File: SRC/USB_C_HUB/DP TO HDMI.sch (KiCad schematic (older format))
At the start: 3 parts

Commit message: ALL DONE BUT THE HDMI SECTION. NEED FOOTPRINT ASSIGNMENT
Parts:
- D11: renamed from D?; footprint DMX0003A -> SamacSys_Parts_2:DMX0003A
- IC2: renamed from IC?; footprint QFN50P700X700X80-49N -> SamacSys_Parts_2:QFN50P700X700X80-49N
- gave numbers to parts that had none: 1
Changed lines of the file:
@@
 $Descr A4 11693 8268
 encoding utf-8
-Sheet 8 11
+Sheet 4 15
 Title ""
 Date ""
@@
 AR Path="/619540C6/64E7C5EF" Ref="#PWR?"  Part="1"
 AR Path="/64E7C5EF" Ref="#PWR?"  Part="1"
-AR Path="/64E160D5/64E7C5EF" Ref="#PWR?"  Part="1"
-F 0 "#PWR?" H 6150 2900 50  0001 C CNN
+AR Path="/64E160D5/64E7C5EF" Ref="#PWR0149"  Part="1"
+F 0 "#PWR0149" H 6150 2900 50  0001 C CNN
 F 1 "GND" H 6155 2977 50  0000 C CNN
 F 2 "" H 6150 3150 60  0000 C CNN
@@
 P 6225 3150
 AR Path="/64E7C5FE" Ref="D?"  Part="1"
-AR Path="/64E160D5/64E7C5FE" Ref="D?"  Part="1"
-F 0 "D?" H 6125 3075 50  0000 C CNN
+AR Path="/64E160D5/64E7C5FE" Ref="D11"  Part="1"
+F 0 "D11" H 6125 3075 50  0000 C CNN
 F 1 "ESD122DMXR" H 6125 3000 50  0000 C CNN
-F 2 "DMX0003A" H 7075 3250 50  0001 L CNN
+F 2 "SamacSys_Parts_2:DMX0003A" H 7075 3250 50  0001 L CNN
 F 3 "http://www.ti.com/lit/gpn/esd122" H 7075 3150 50  0001 L CNN
 F 4 "2-Channel ESD Protection Diode for USB Type-C and HDMI 2.0" H 7075 3050 50  0001 L CNN "Description"
@@
 P 8175 3625
 AR Path="/64E7C620" Ref="#PWR?"  Part="1"
-AR Path="/64E160D5/64E7C620" Ref="#PWR?"  Part="1"
-F 0 "#PWR?" H 8175 3475 50  0001 C CNN
+AR Path="/64E160D5/64E7C620" Ref="#PWR0150"  Part="1"
+F 0 "#PWR0150" H 8175 3475 50  0001 C CNN
 F 1 "+5V" V 8190 3753 50  0000 L CNN
 F 2 "" H 8175 3625 60  0000 C CNN
@@
 P 8575 2850
 AR Path="/64E7C627" Ref="HDMI?"  Part="1"
-AR Path="/64E160D5/64E7C627" Ref="HDMI?"  Part="1"
-F 0 "HDMI?" H 8431 2804 50  0000 R CNN
+AR Path="/64E160D5/64E7C627" Ref="HDMI1"  Part="1"
+F 0 "HDMI1" H 8431 2804 50  0000 R CNN
 F 1 "HDMI-SWM-19" H 8431 2895 50  0000 R CNN
 F 2 "" H 8605 3000 20  0001 C CNN
@@
 P 8900 1775
 AR Path="/64E7C634" Ref="#PWR?"  Part="1"
-AR Path="/64E160D5/64E7C634" Ref="#PWR?"  Part="1"
-F 0 "#PWR?" H 8900 1525 50  0001 C CNN
+AR Path="/64E160D5/64E7C634" Ref="#PWR0151"  Part="1"
+F 0 "#PWR0151" H 8900 1525 50  0001 C CNN
 F 1 "GND" H 8905 1602 50  0000 C CNN
 F 2 "" H 8900 1775 60  0000 C CNN
@@
 P 8625 4025
 AR Path="/64E7C63A" Ref="#PWR?"  Part="1"
-AR Path="/64E160D5/64E7C63A" Ref="#PWR?"  Part="1"
-F 0 "#PWR?" H 8625 3775 50  0001 C CNN
+AR Path="/64E160D5/64E7C63A" Ref="#PWR0152"  Part="1"
+F 0 "#PWR0152" H 8625 3775 50  0001 C CNN
 F 1 "GND" H 8725 3900 50  0000 C CNN
 F 2 "" H 8625 4025 60  0000 C CNN
@@
 P 3200 4075
 AR Path="/64E7C666" Ref="IC?"  Part="1"
-AR Path="/64E160D5/64E7C666" Ref="IC?"  Part="1"
-F 0 "IC?" V 4150 3550 50  0000 C CNN
+AR Path="/64E160D5/64E7C666" Ref="IC2"  Part="1"
+F 0 "IC2" V 4150 3550 50  0000 C CNN
 F 1 "MAX9406ETM+T" V 4025 3500 50  0000 C CNN
-F 2 "QFN50P700X700X80-49N" H 4850 4575 50  0001 L CNN
+F 2 "SamacSys_Parts_2:QFN50P700X700X80-49N" H 4850 4575 50  0001 L CNN
 F 3 "https://pdfserv.maximintegrated.com/en/ds/MAX9406.pdf" H 4850 4475 50  0001 L CNN
 F 4 "MAX9406ETM+T" H 4850 4375 50  0001 L CNN "Description"

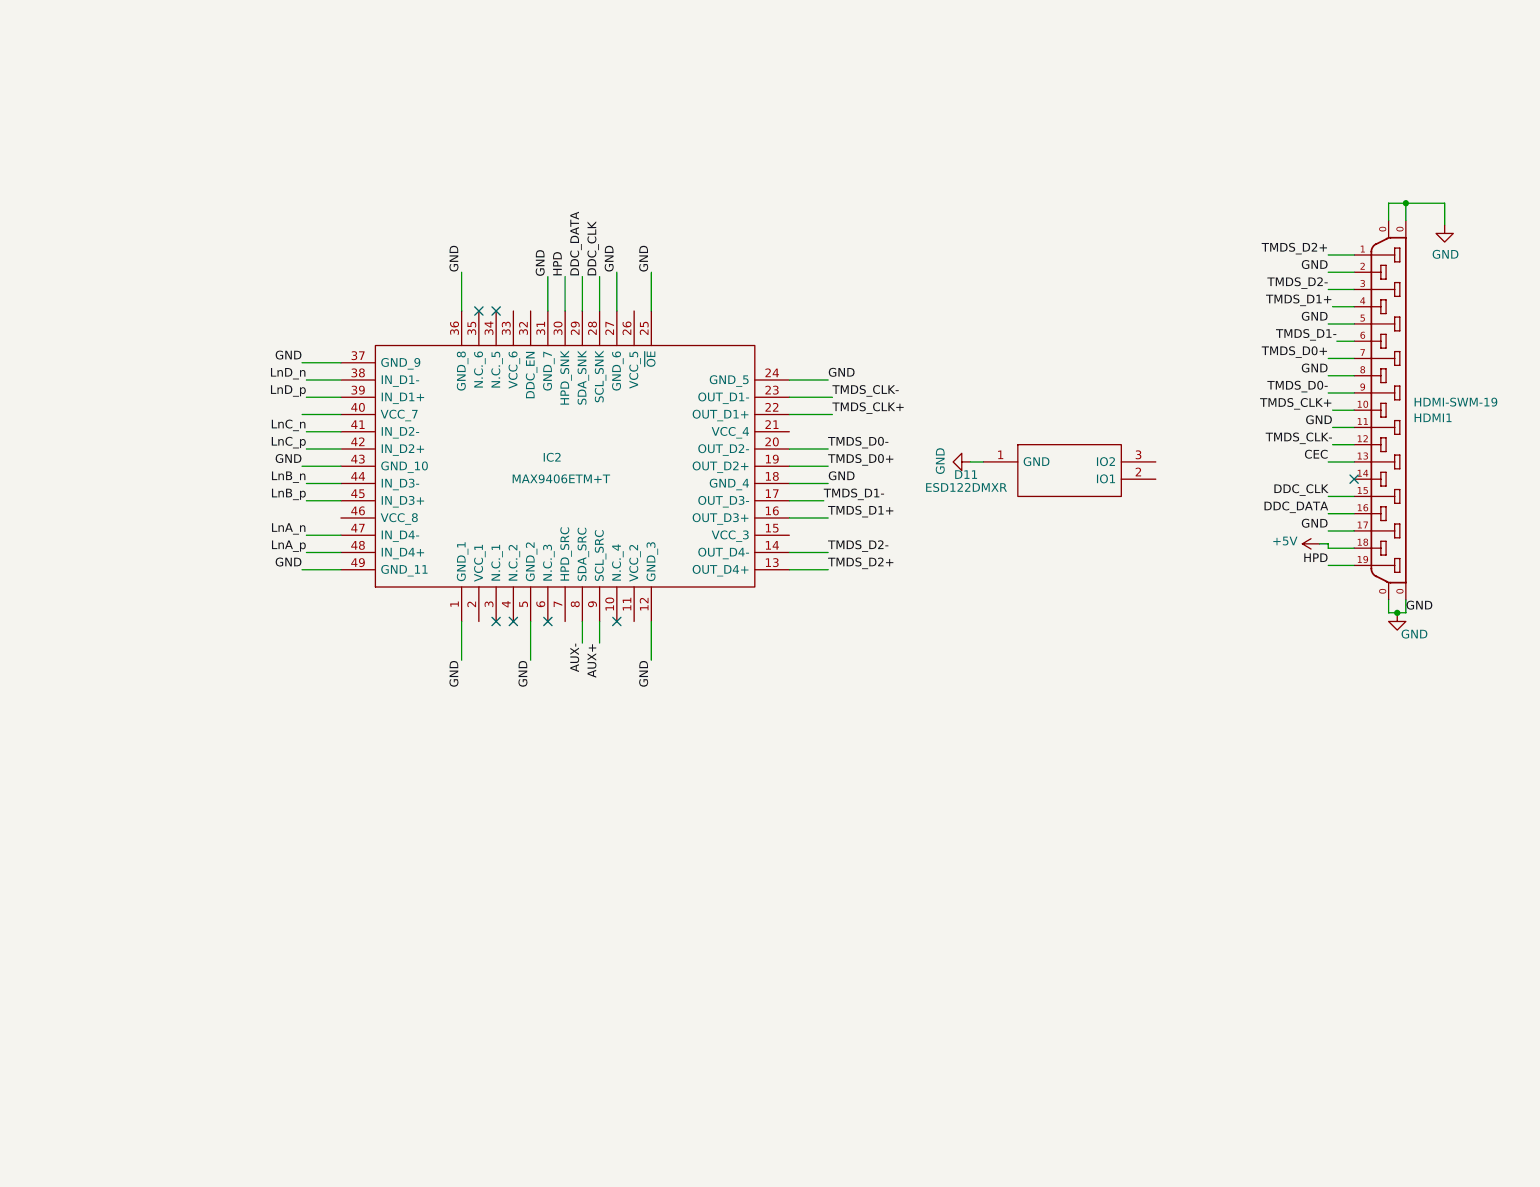
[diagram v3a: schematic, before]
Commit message: schematic capture complete. Pending Footprint assignment. accetable Errors=21
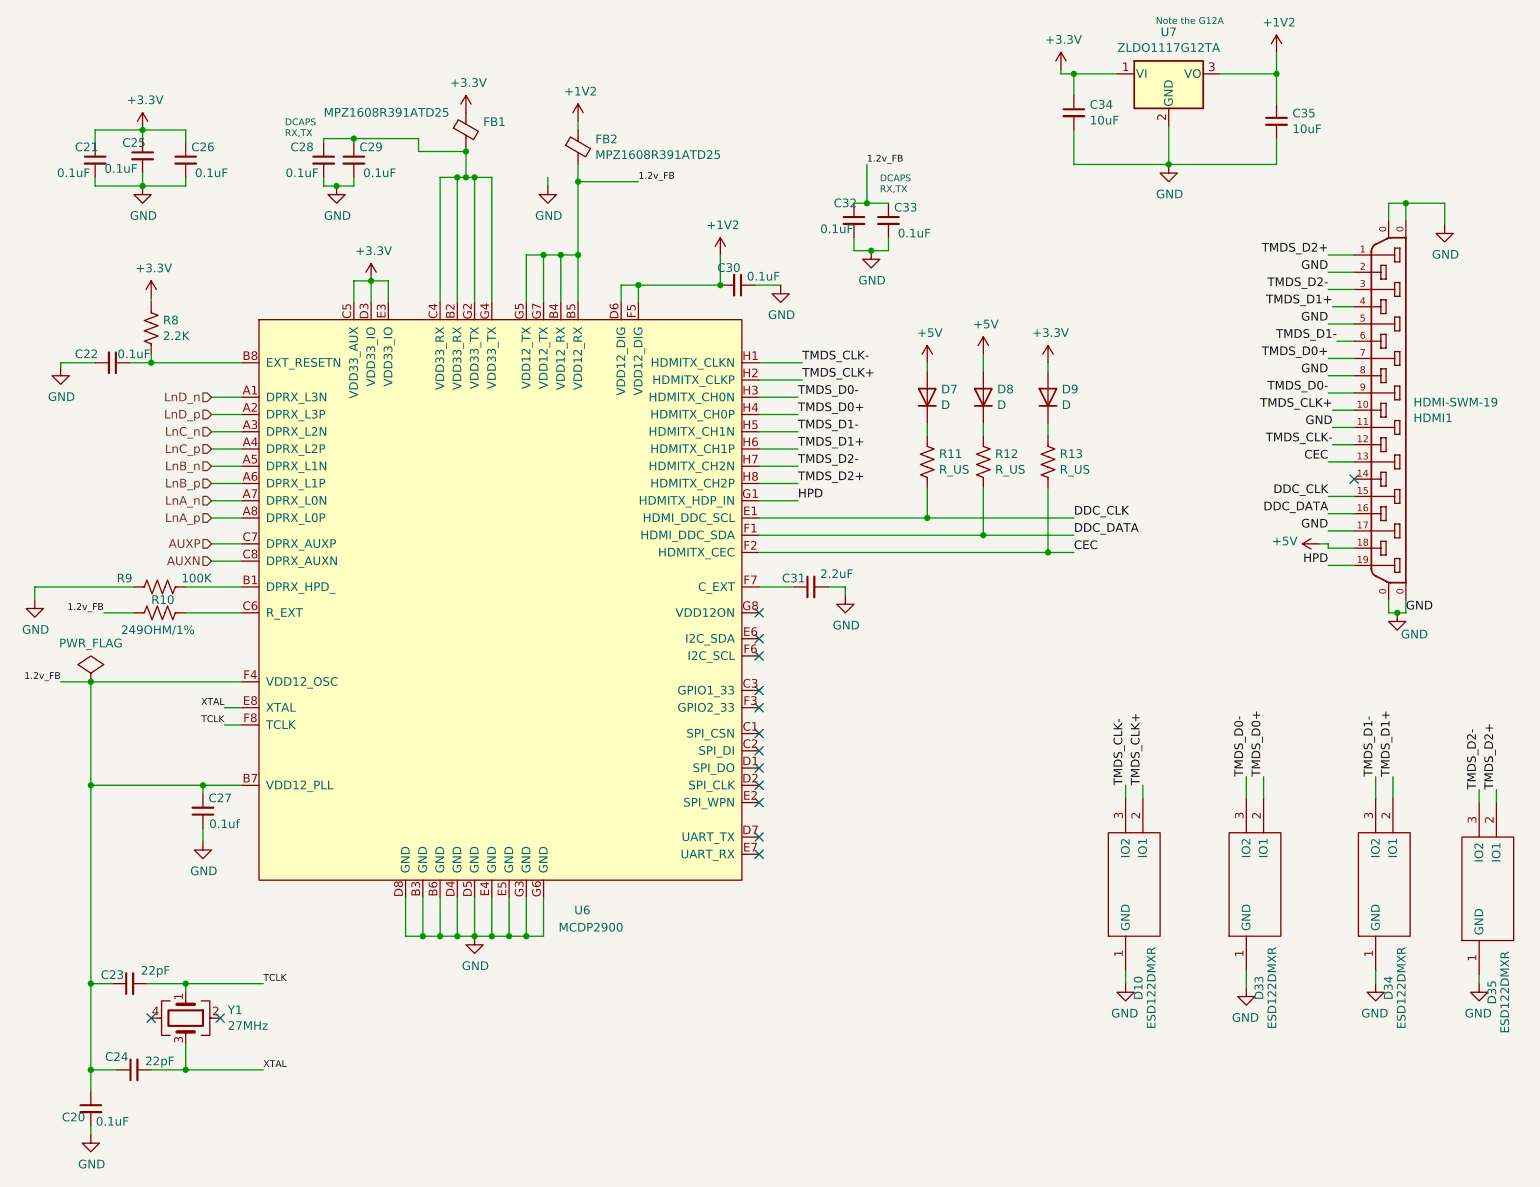
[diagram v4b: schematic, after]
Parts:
- removed IC2: MAX9406ETM+T, SamacSys_Parts_2:QFN50P700X700X80-49N, symbol SamacSys_Parts:MAX9406ETM+T
- added C20, C21, C22, C25, C26, C28, C29, C30, C32, C33: 0.1uF, symbol Device:C_Small
- added C23, C24: 22pF, symbol Device:C_Small
- added C27: 0.1uf, symbol Device:C_Small
- added C31: 2.2uF, symbol Device:C_Small
- added C34, C35: 10uF, symbol Device:C_Small
- added D33, D34, D35: ESD122DMXR, SamacSys_Parts_2:DMX0003A, symbol SamacSys_Parts:ESD122DMXR
- added D7, D8, D9: D, symbol Device:D
- added FB1, FB2: MPZ1608R391ATD25, Resistor_SMD:R_0603_1608Metric, symbol Device:Ferrite_Bead_Small
- added R10: 249OHM/1%, symbol Device:R_US
- added R11, R12, R13: R_US, symbol Device:R_US
- added R8: 2.2K, symbol Device:R_US
- added R9: 100K, symbol Device:R_US
- added U6: MCDP2900, symbol usb_hub:MCDP2900
- added U7: ZLDO1117G12TA, Package_TO_SOT_SMD:SOT-223-3_TabPin2, symbol Regulator_Linear:LF85_TO220
- added Y1: 27MHz, symbol Device:Crystal_GND24
- renumbered D11 to D10
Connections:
- net +5V: now also D7.2 (A), D8.2 (A)
- net CEC: now also R13.2, U6.F2 (HDMITX_CEC)
- net DDC_CLK: now also R11.2, U6.E1 (HDMI_DDC_SCL)
- net DDC_DATA: now also R12.2, U6.F1 (HDMI_DDC_SDA)
- net GND: now also C20.2, C21.2, C22.2, C25.2, C26.2, C27.1, C28.2, C29.2, C30.1, C31.2, C32.2, C33.2, C34.2, C35.2, D33.1 (GND), D34.1 (GND), D35.1 (GND), R9.2, U6.B3 (GND), U6.B6 (GND), U6.D4 (GND), U6.D5 (GND), U6.D8 (GND), U6.E4 (GND), U6.E5 (GND), U6.G3 (GND), U6.G6 (GND), U7.2 (GND)
- net HPD: now also U6.G1 (HDMITX_HDP_IN)
- net LnA_n: now also U6.A7 (DPRX_L0N)
- net LnA_p: now also U6.A8 (DPRX_L0P)
- net LnB_n: now also U6.A5 (DPRX_L1N)
- net LnB_p: now also U6.A6 (DPRX_L1P)
- net LnC_n: now also U6.A3 (DPRX_L2N)
- net LnC_p: now also U6.A4 (DPRX_L2P)
- net LnD_n: now also U6.A1 (DPRX_L3N)
- net LnD_p: now also U6.A2 (DPRX_L3P)
- net TMDS_CLK+: now also D10.2 (IO1), U6.H2 (HDMITX_CLKP)
- net TMDS_CLK-: now also D10.3 (IO2), U6.H1 (HDMITX_CLKN)
- net TMDS_D0+: now also D33.2 (IO1), U6.H4 (HDMITX_CH0P)
- net TMDS_D0-: now also D33.3 (IO2), U6.H3 (HDMITX_CH0N)
- net TMDS_D1+: now also D34.2 (IO1), U6.H6 (HDMITX_CH1P)
- net TMDS_D1-: now also D34.3 (IO2), U6.H5 (HDMITX_CH1N)
- net TMDS_D2+: now also D35.2 (IO1), U6.H8 (HDMITX_CH2P)
- net TMDS_D2-: now also D35.3 (IO2), U6.H7 (HDMITX_CH2N)
- new net: C22.1, R8.2, U6.B8 (EXT_RESETN)
- new net: R9.1, U6.B1 (DPRX_HPD_)
- new net: C28.1, C29.1, FB1.2, U6.B2 (VDD33_RX), U6.C4 (VDD33_RX), U6.G2 (VDD33_TX), U6.G4 (VDD33_TX)
- new net: R10.1, U6.C6 (R_EXT)
- new net: C31.1, U6.F7 (C_EXT)
- new net: D7.1 (K), R11.1
- new net: D8.1 (K), R12.1
- new net: D9.1 (K), R13.1
- new net +1V2: C30.2, C35.1, FB2.1, U6.D6 (VDD12_DIG), U6.F5 (VDD12_DIG), U7.3 (VO)
- new net +3V3: C21.1, C25.1, C26.1, C34.1, D9.2 (A), FB1.1, R8.1, U6.C5 (VDD33_AUX), U6.D3 (VDD33_IO), U6.E3 (VDD33_IO), U7.1 (VI)
- new net 1.2v_FB: C20.1, C23.1, C24.1, C27.2, C32.1, C33.1, FB2.2, R10.2, U6.B4 (VDD12_RX), U6.B5 (VDD12_RX), U6.B7 (VDD12_PLL), U6.F4 (VDD12_OSC), U6.G5 (VDD12_TX), U6.G7 (VDD12_TX)
- new net AUXN: U6.C8 (DPRX_AUXN)
- new net AUXP: U6.C7 (DPRX_AUXP)
- new net TCLK: C23.2, U6.F8 (TCLK), Y1.1
- new net XTAL: C24.2, U6.E8 (XTAL), Y1.3
- no-connect marks 7 -> 15
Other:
- note added: "DCAPS\nRX,TX"
- note added: "Note the G12A"
- moved on the sheet: D10
